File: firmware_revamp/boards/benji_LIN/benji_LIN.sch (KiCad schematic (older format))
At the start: 37 parts, among them J1 CONN_02X03, J2 Conn_01x09, J3 Conn_01x09, J4 CONN_01X03, J5 CONN_01x02, J6 CONN_01X03, J7 CONN_01x02, U1 MCP2561-E_SN, U2 ATMEGA16M1, U3 TLIN1021DRQ1, Y1 Crystal_SMD

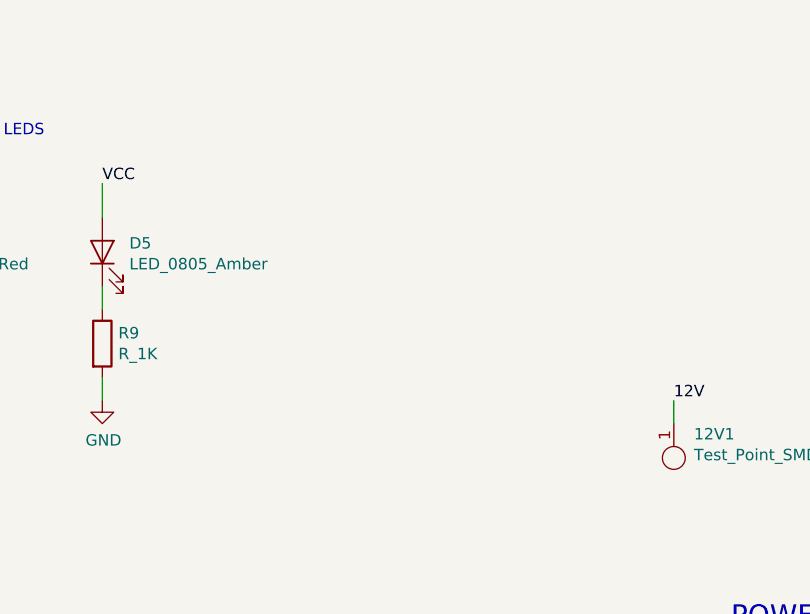
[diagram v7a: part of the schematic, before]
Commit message: Added 12v Led to schematic
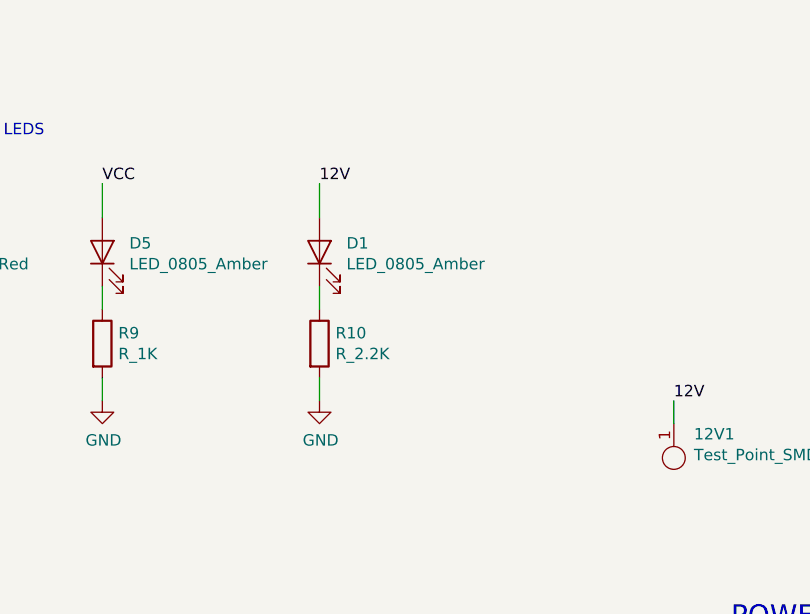
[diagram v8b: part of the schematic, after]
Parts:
- added D1: LED_0805_Amber, footprints:LED_0805_OEM, symbol formula:LED_0805_Amber
- added R10: R_2.2K, footprints:R_0805_OEM, symbol formula:R_2.2K
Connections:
- net 12V: now also D1.2 (A)
- net GND: now also R10.2
- new net: D1.1 (K), R10.1
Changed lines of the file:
@@
 	1    0    0    -1
 $EndComp
+$Comp
+L formula:R_2.2K R10
+U 1 1 60713089
+P 10650 5950
+F 0 "R10" H 10720 5996 50  0000 L CNN
+F 1 "R_2.2K" H 10720 5905 50  0000 L CNN
+F 2 "footprints:R_0805_OEM" H 10580 5950 50  0001 C CNN
+F 3 "https://www.seielect.com/Catalog/SEI-RMCF_RMCP.pdf" H 10730 5950 50  0001 C CNN
+F 4 "DK" H 10650 5950 60  0001 C CNN "MFN"
+F 5 "RMCF0805FT2K20CT-ND" H 10650 5950 60  0001 C CNN "MPN"
+F 6 "https://www.digikey.com/product-detail/en/stackpole-electronics-inc/RMCF0805FT2K20/RMCF0805FT2K20CT-ND/1942387" H 11130 6350 60  0001 C CNN "PurchasingLink"
+	1    10650 5950
+	1    0    0    -1
+$EndComp
+$Comp
+L power:GND #PWR0103
+U 1 1 60715E33
+P 10650 6200
+F 0 "#PWR0103" H 10650 5950 50  0001 C CNN
+F 1 "GND" H 10655 6027 50  0000 C CNN
+F 2 "" H 10650 6200 50  0001 C CNN
+F 3 "" H 10650 6200 50  0001 C CNN
+	1    10650 6200
+	1    0    0    -1
+$EndComp
+Wire Wire Line
+	10650 6100 10650 6200
+Wire Wire Line
+	10650 5700 10650 5800
+$Comp
+L formula:LED_0805_Amber D1
+U 1 1 6072AB92
+P 10650 5550
+F 0 "D1" V 10689 5432 50  0000 R CNN
+F 1 "LED_0805_Amber" V 10598 5432 50  0000 R CNN
+F 2 "footprints:LED_0805_OEM" H 10550 5550 50  0001 C CNN
+F 3 "https://media.digikey.com/pdf/Data%20Sheets/Chicago%20Miniature%20Lamps%20PDFs/CMDA5_Series_Rev_Aug_2014.pdf" H 10650 5650 50  0001 C CNN
+F 4 "DK" H 10650 5550 60  0001 C CNN "MFN"
+F 5 "L71517CT-ND" H 10650 5550 60  0001 C CNN "MPN"
+F 6 "https://www.digikey.com/product-detail/en/visual-communications-company-vcc/CMDA5DY7D1S/L71517CT-ND/614867" H 11050 6050 60  0001 C CNN "PurchasingLink"
+	1    10650 5550
+	0    -1   -1   0
+$EndComp
+Text Label 10650 5250 0    50   ~ 0
+12V
+Wire Wire Line
+	10650 5250 10650 5400
 $EndSCHEMATC
